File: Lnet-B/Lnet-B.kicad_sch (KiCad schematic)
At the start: 13 parts, among them J601 RJ12, J602 RJ12, Q601 NPN_TOR, U601 LM311

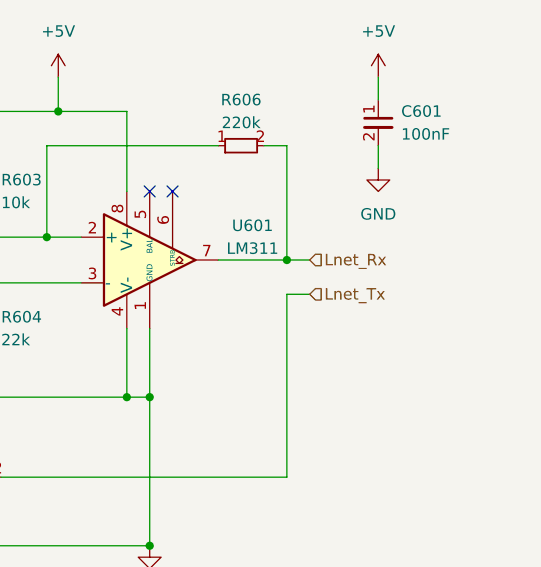
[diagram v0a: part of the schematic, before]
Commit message: made some hierarchial label changes and updated atmega328
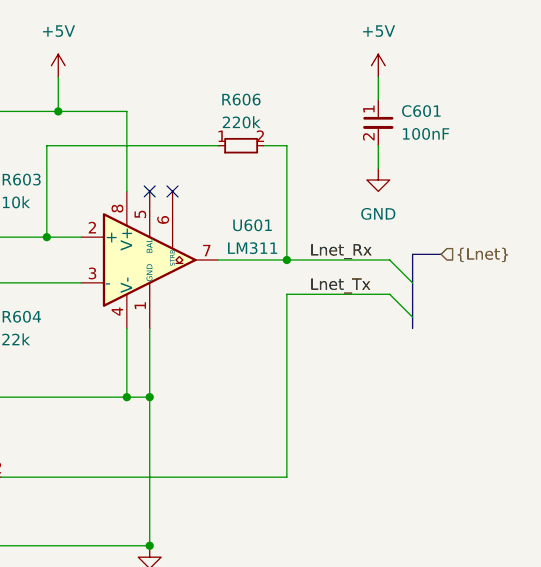
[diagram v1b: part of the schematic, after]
